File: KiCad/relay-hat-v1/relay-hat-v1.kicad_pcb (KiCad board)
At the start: 2 copper layers, 99.3 x 47.5 mm, 57 parts, among them J1 Screw_Terminal_01x04, J2 Conn_01x04_Pin, M1 Fan, U1 TCA9554PW, U10 TMP1075DGKR, U11 LM311, U12 TPS2051CDBV, U2 TPS2051CDBV, U3 TPS2051CDBV, U4 TPS2051CDBV, U5 TPS2051CDBV, U6 TPS2051CDBV, U7 TPS2000CDGK, U8 TPS2000CDGK, U9 TPS2000CDGK

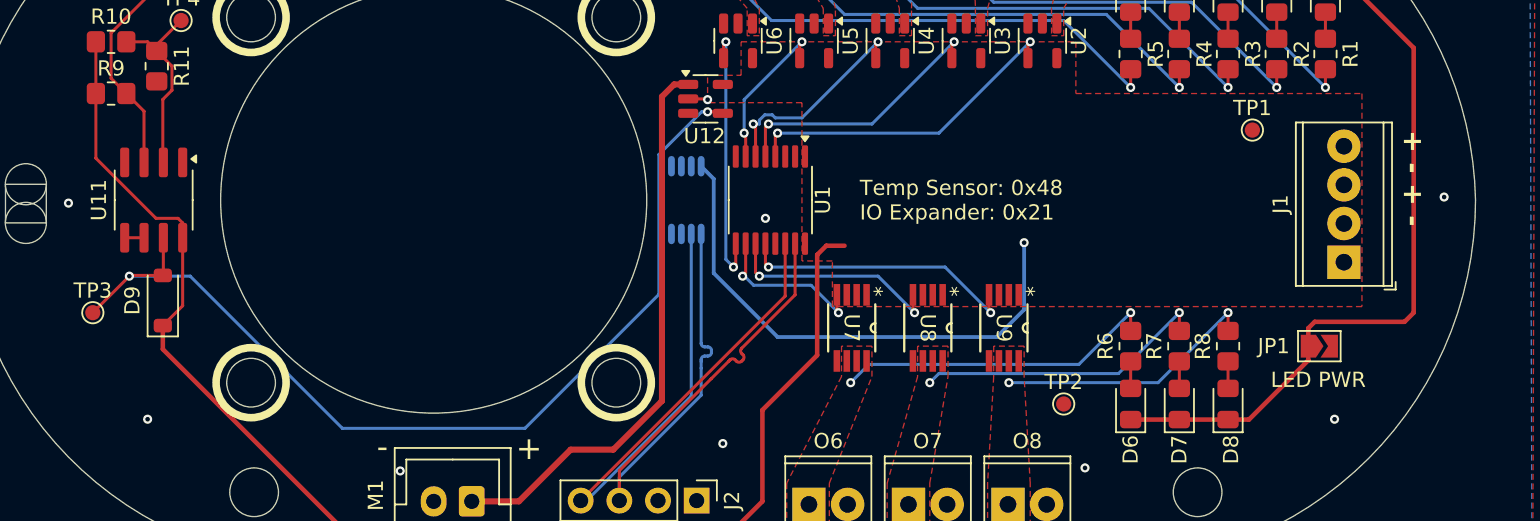
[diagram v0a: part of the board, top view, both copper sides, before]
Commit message: Test code and changed diode for resistor
The diode after the op-amp on the relay board is now a 10K pullup resistor
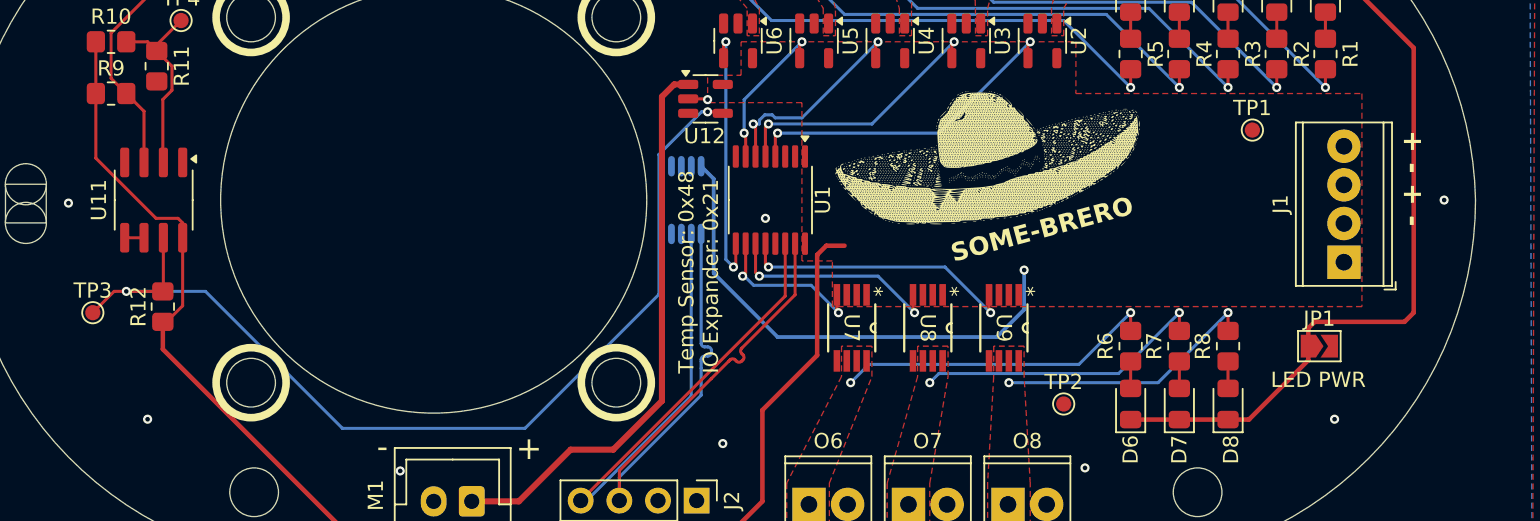
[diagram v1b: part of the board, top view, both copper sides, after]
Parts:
- removed D9: 1N4148, Diode_SMD:D_SOD-123
- added G***: LOGO, LOGO, F.Cu at (184.2, 66.2)
- added R12: 10k, Resistor_SMD:R_0805_2012Metric_Pad1.20x1.40mm_HandSolder, F.Cu at (130.0, 76.0)
- JP1: value SolderJumper_2_Open -> SolderJumper_2_Closed
- R1, R2, R3, R4, R5, R6, R7, R8: value 120 -> 820
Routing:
- net +5V: track 123.5 -> 121.7 mm
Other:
- board text added: "For when you only want SOME things on..."
- board text added: "SOME-BRERO"
